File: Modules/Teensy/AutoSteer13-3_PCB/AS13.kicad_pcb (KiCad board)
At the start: 2 copper layers, 159 x 159 mm, 90 parts, among them IC1 AZ1117, IC2 XL2596, J1 U-USBAS04P-F000, J10 I2C-3V3, J11 I2C-3V3, J12 Conn_02x02_Counter_Clockwise, J13 Conn_01x15_Female, J14 Conn_01x08_Female, J15 BNO080_left, J16 BNO080_right, J17 Conn_01x15_Female, J18 Conn_01x08_Female, J19 Motor 2, J2 RS485, J20 Motor 1, J21 SF_F9P_left, J22 ArduSimple_tl, J23 ArduSimple_bl, J24 SF_F9P_right, J25 ArduSimple_tr, J26 ArduSimple_br, J27 Grove, J3 Teensy_USBhost, J4 HR911105A, J5 PM254V-11-06-H85, J6 DT13-12PA, J7 WemosD1_left, J8 Teensy_Ethernet, J9 WemosD1_right, K1 SRD-05VDC-SL-C, M1 CMPS14, Q1 BC847, U1 SP3485EN-L/TR, U2 PC817X2CSP9F, U3 PC817X2CSP9F, U4 PC817X2CSP9F, U5 PC817X2CSP9F, U6 CC6900SO-10A

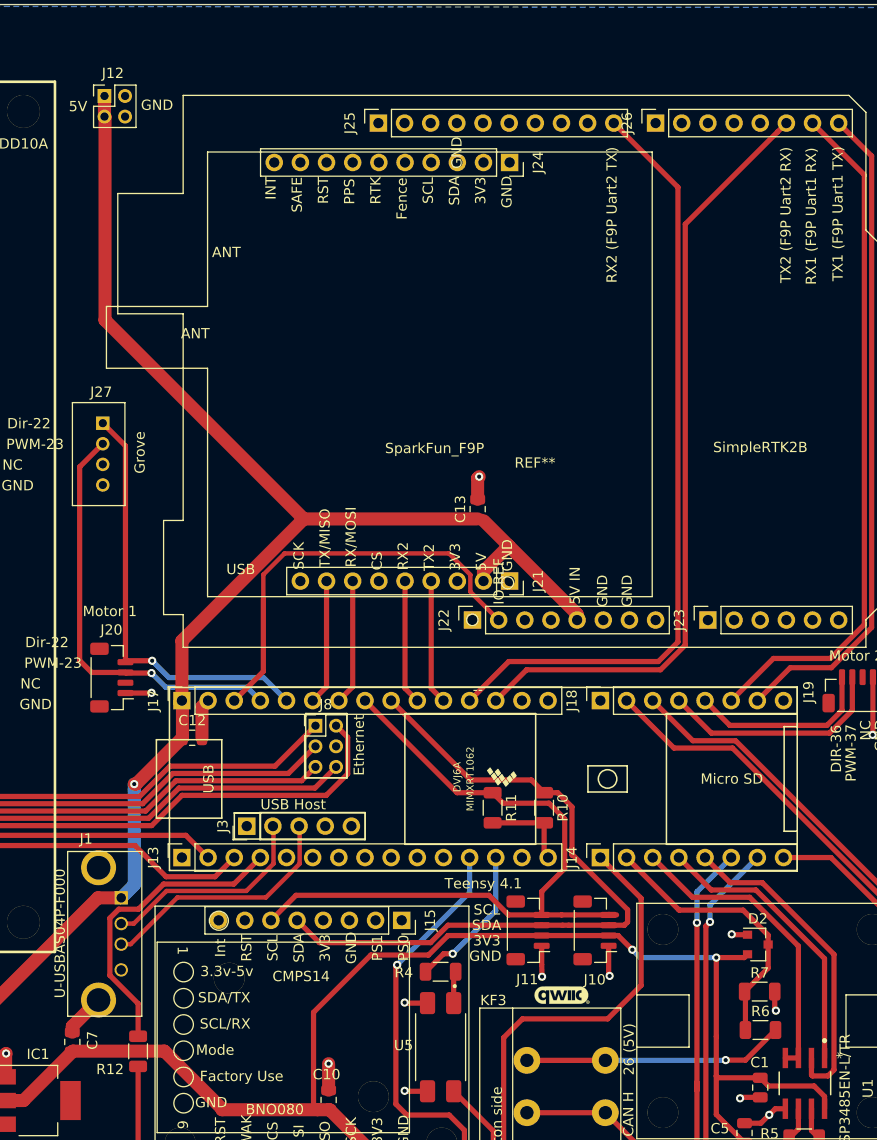
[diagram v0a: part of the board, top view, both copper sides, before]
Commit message: fixed the RS485 circuit
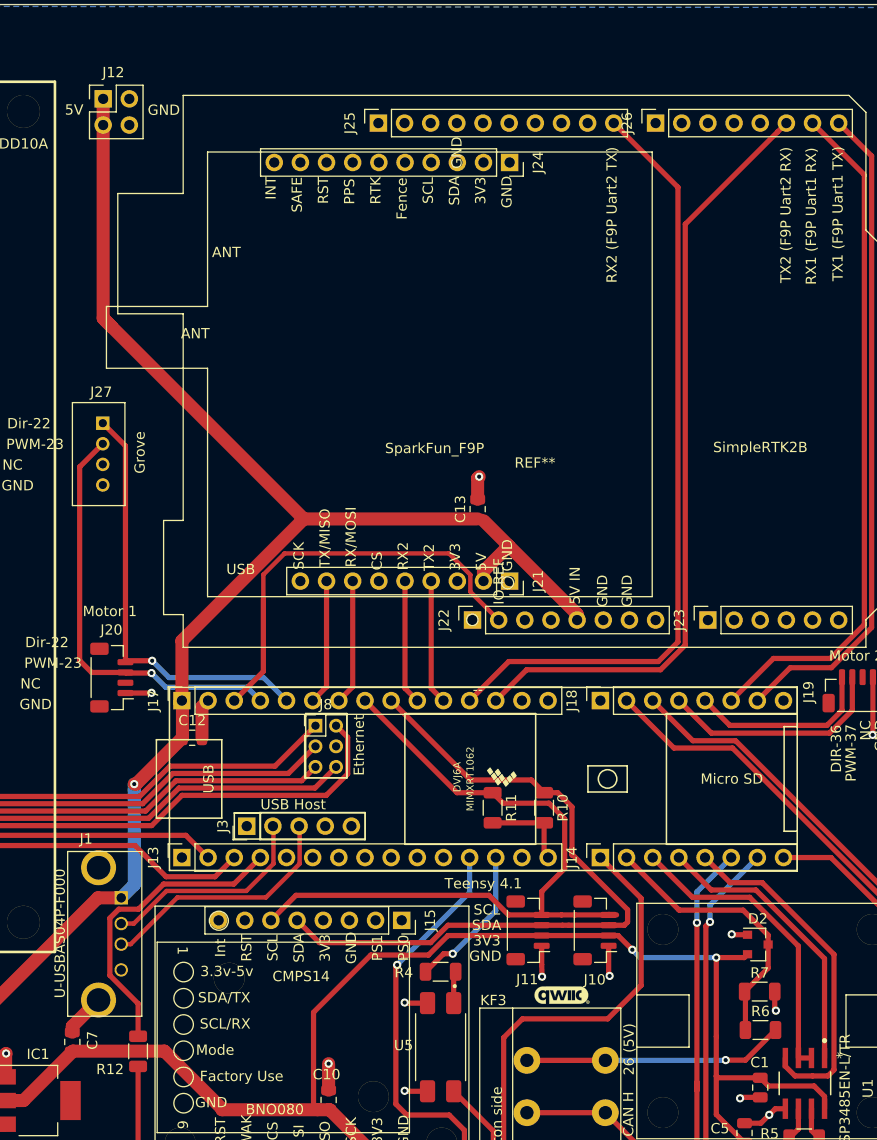
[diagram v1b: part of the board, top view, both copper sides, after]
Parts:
- J12: footprint Connector_PinSocket_2.00mm:PinSocket_2x02_P2.00mm_Vertical -> Connector_PinSocket_2.54mm:PinSocket_2x02_P2.54mm_Vertical
- moved J12 0.31 mm to (94.2, 29.2)
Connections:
- U1 pad 2: Net-(J14-Pad5) -> Net-(J14-Pad3)
- U1 pad 4: Net-(J14-Pad3) -> Net-(J14-Pad5)
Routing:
- net Net-(J14-Pad5): track 31.7 -> 33.8 mm
- net Net-(C11-Pad1): track 431.8 -> 432.5 mm
